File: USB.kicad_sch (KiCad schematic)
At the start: 1 part

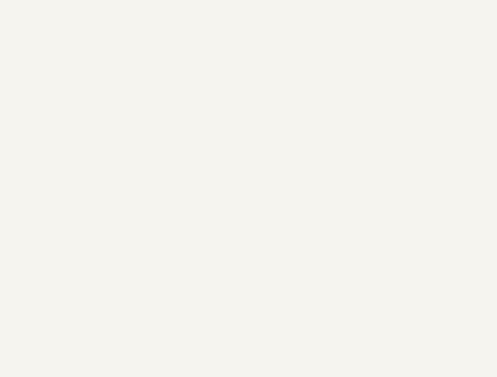
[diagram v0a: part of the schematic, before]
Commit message: updated titles and changes to wires
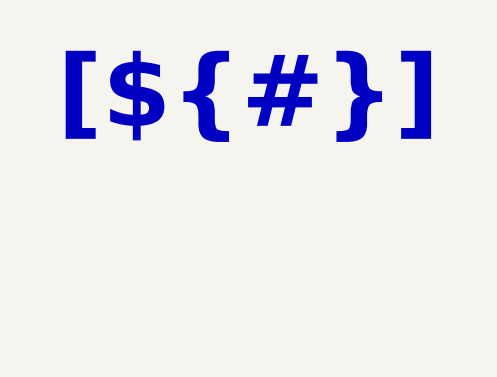
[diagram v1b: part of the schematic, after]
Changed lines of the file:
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@@
 	(generator_version "9.0")
 	(paper "A4")
+	(text_box "[${#}] ${TITLE}"
+		(exclude_from_sim no)
+		(at 88.9 20.828 0)
+		(size 130.81 12.7)
+		(margins 5.9999 5.9999 5.9999 5.9999)
+		(stroke
+			(width -0.0001)
+			(type default)
+		)
+		(fill
+			(type none)
+		)
+		(effects
+			(font
+				(face "Times New Roman")
+				(size 8 8)
+				(thickness 1.2)
+				(bold yes)
+				(color 162 22 34 1)
+			)
+		)
+	)
 	(junction
 		(at 158.75 95.25)

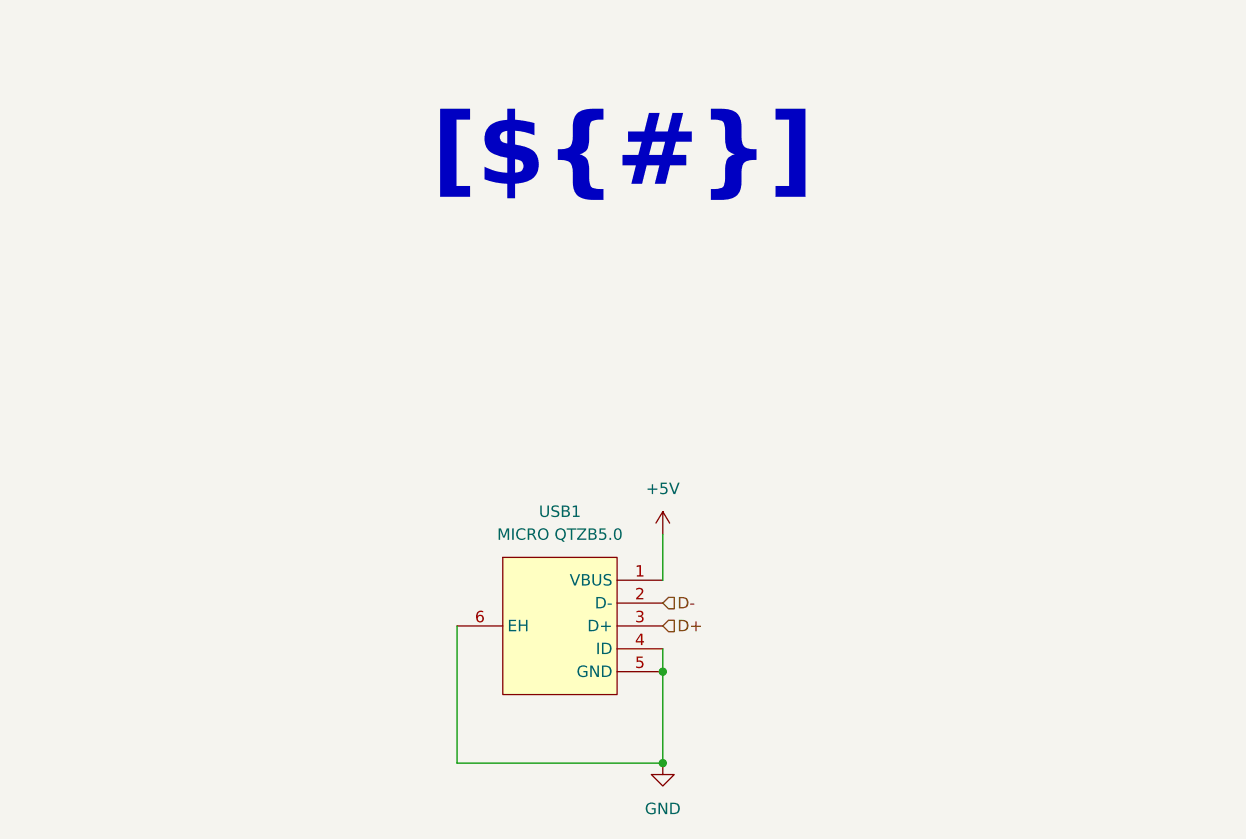
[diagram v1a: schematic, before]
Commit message: updated titles and changes to wires
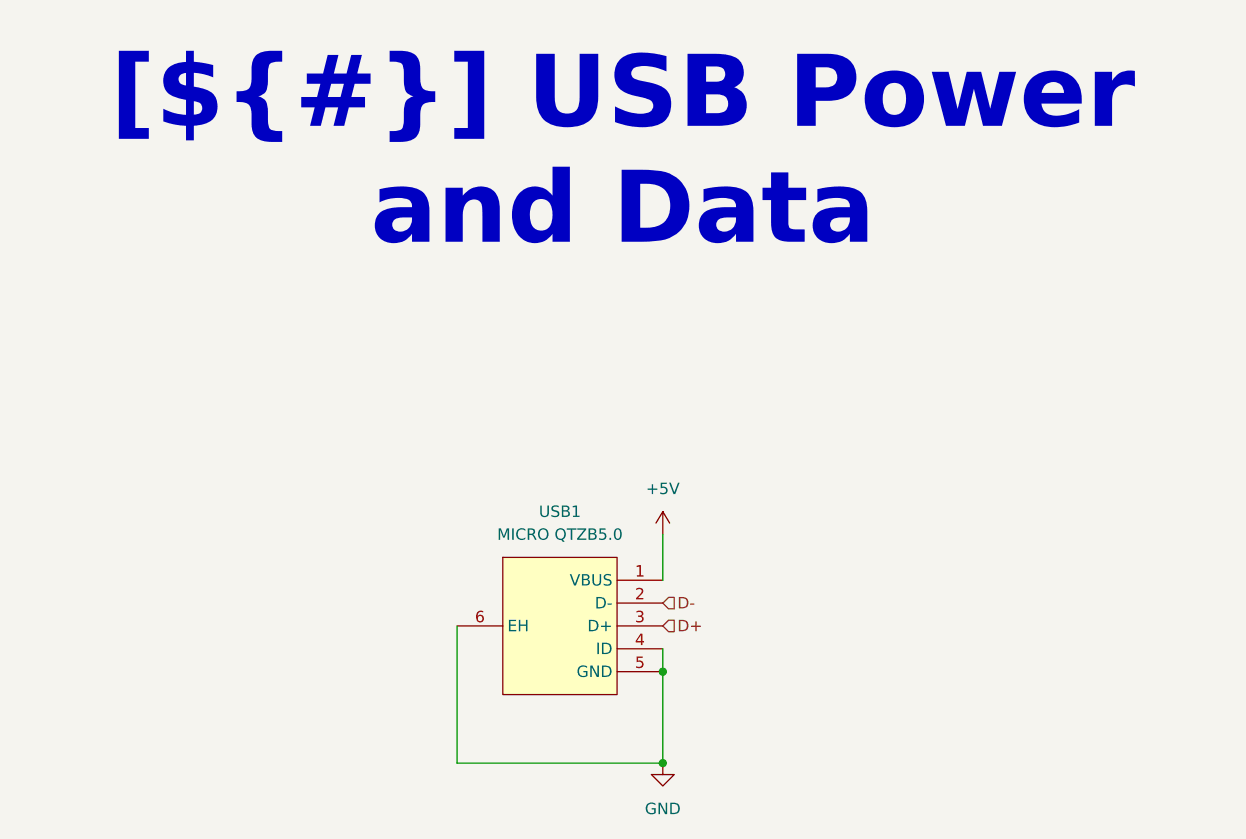
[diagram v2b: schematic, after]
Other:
- title: (none) -> USB Power and Data
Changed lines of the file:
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@@
 	(generator_version "9.0")
 	(paper "A4")
+	(title_block
+		(title "USB Power and Data")
+	)
 	(text_box "[${#}] ${TITLE}"
 		(exclude_from_sim no)
